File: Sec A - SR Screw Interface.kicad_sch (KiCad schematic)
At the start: 1 part, among them U1 B-B Interface

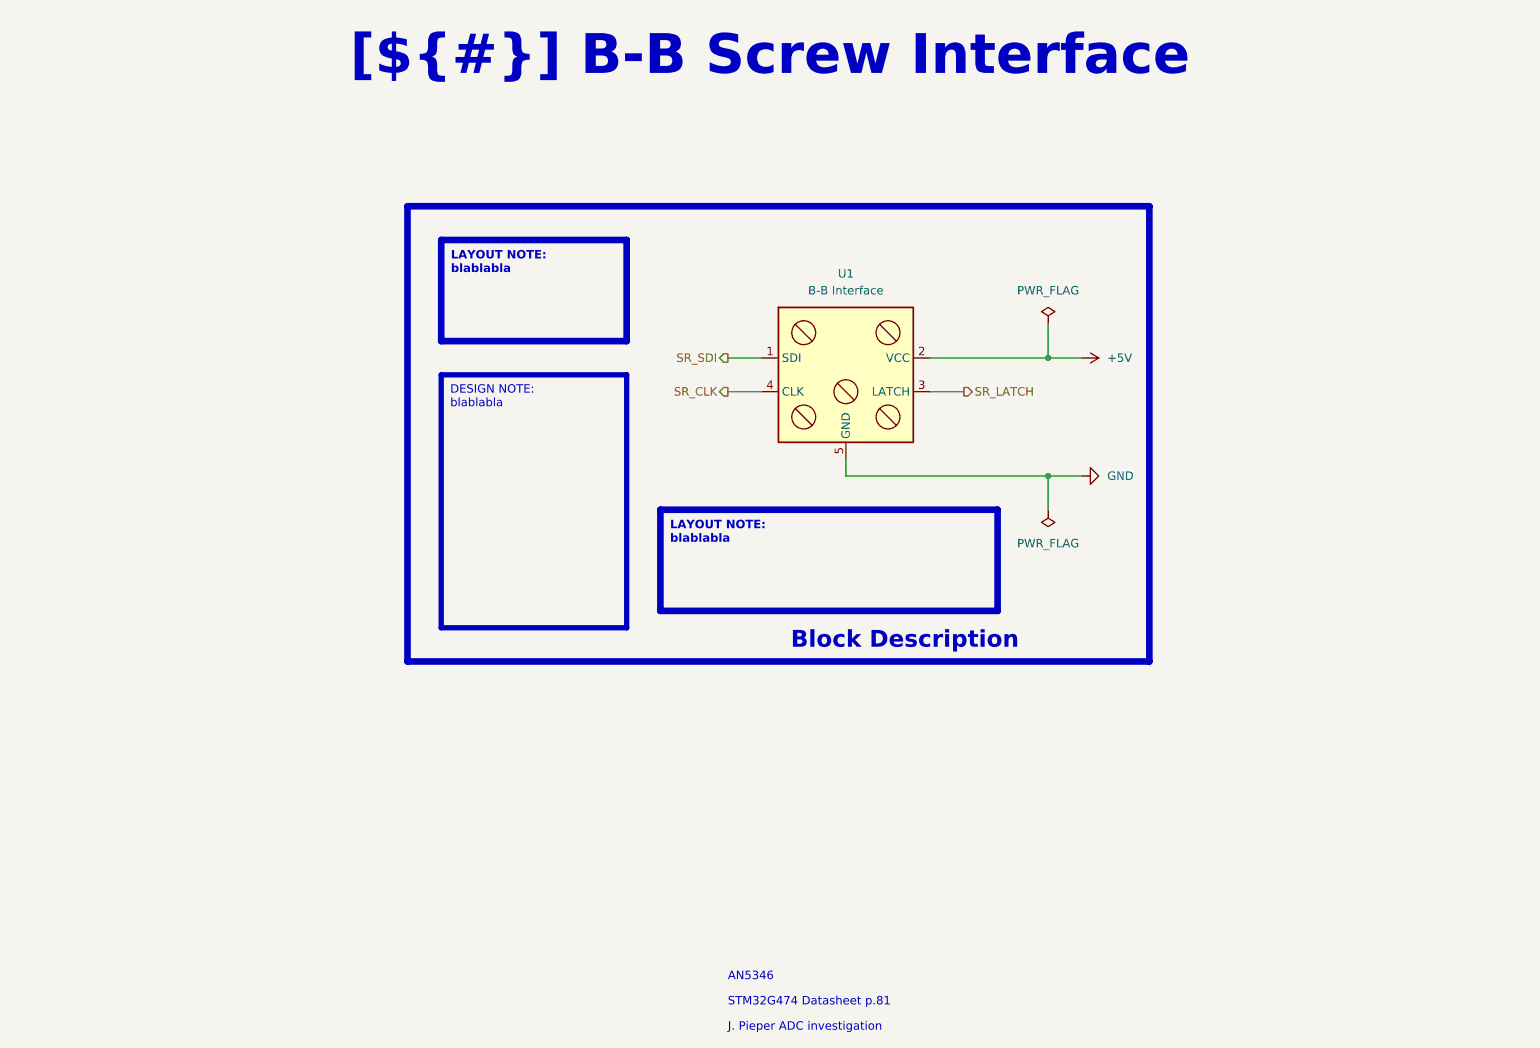
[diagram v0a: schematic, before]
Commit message: documentation update / release 2.1.1 prep
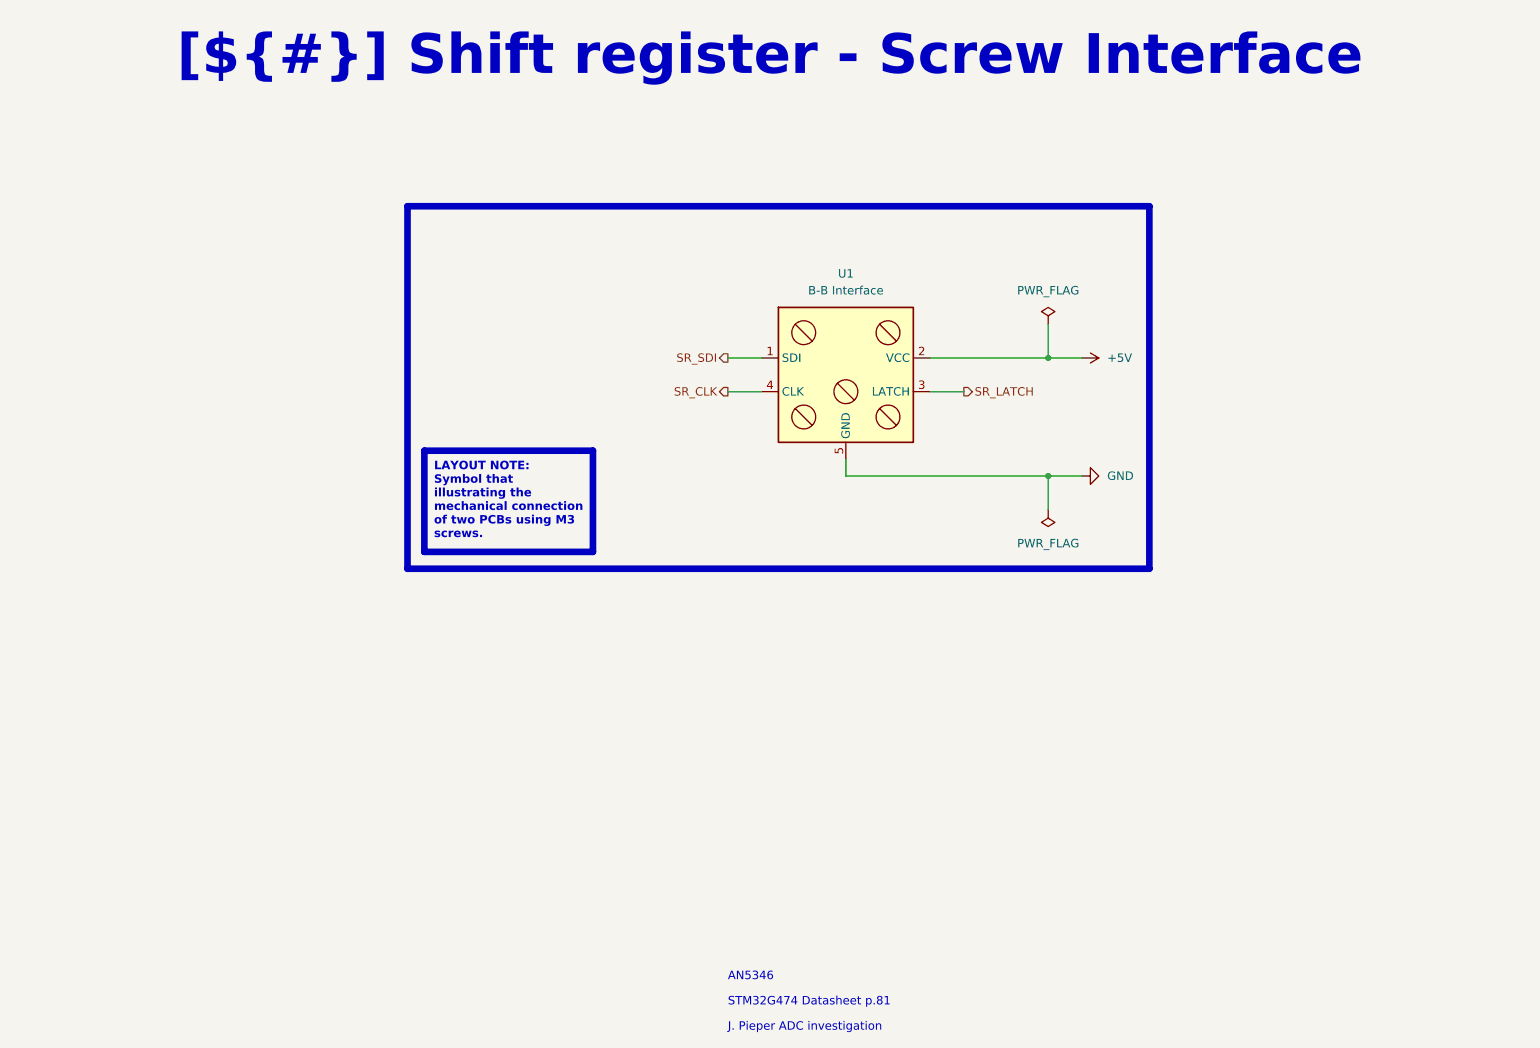
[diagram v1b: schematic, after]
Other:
- title: B-B Screw Interface -> Shift register - Screw Interface
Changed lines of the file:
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@@
 	(paper "A4")
 	(title_block
-		(title "B-B Screw Interface")
+		(title "Shift register - Screw Interface")
 		(date "2025-01-12")
 		(rev "${REVISION}")
@@
 	(rectangle
 		(start 93.98 45.72)
-		(end 205.74 114.3)
+		(end 205.74 100.33)
 		(stroke
 			(width 1)
@@
 		)
 	)
-	(text_box "Block Description"
+	(text_box "LAYOUT NOTE:\nSymbol that illustrating the mechanical connection of two PCBs using M3 screws."
 		(exclude_from_sim no)
-		(at 132.08 106.68 0)
-		(size 73.66 7.62)
-		(margins 1.9049 1.9049 1.9049 1.9049)
-		(stroke
-			(width -0.0001)
-			(type default)
-		)
-		(fill
-			(type none)
-		)
-		(effects
-			(font
-				(face "Times New Roman")
-				(size 2.54 2.54)
-				(thickness 0.508)
-				(bold yes)
-				(color 162 22 34 1)
-			)
-			(justify bottom)
-		)
-	)
-	(text_box "LAYOUT NOTE:\nblablabla"
-		(exclude_from_sim no)
-		(at 132.08 91.44 0)
-		(size 50.8 15.24)
-		(margins 1.4525 1.4525 1.4525 1.4525)
-		(stroke
-			(width 1)
-			(type solid)
-			(color 0 0 255 1)
-		)
-		(fill
-			(type none)
-		)
-		(effects
-			(font
-				(face "Arial")
-				(size 1.27 1.27)
-				(thickness 0.4)
-				(bold yes)
-				(color 0 0 255 1)
-			)
-			(justify left top)
-		)
-	)
-	(text_box "LAYOUT NOTE:\nblablabla"
-		(exclude_from_sim no)
-		(at 99.06 50.8 0)
-		(size 27.94 15.24)
+		(at 96.52 82.55 0)
+		(size 25.4 15.24)
 		(margins 1.4525 1.4525 1.4525 1.4525)
 		(stroke
@@
 		)
 	)
-	(text_box "DESIGN NOTE:\nblablabla"
-		(exclude_from_sim no)
-		(at 99.06 71.12 0)
-		(size 27.94 38.1)
-		(margins 1.3525 1.3525 1.3525 1.3525)
-		(stroke
-			(width 0.8)
-			(type solid)
-			(color 250 236 0 1)
-		)
-		(fill
-			(type none)
-		)
-		(effects
-			(font
-				(face "Arial")
-				(size 1.27 1.27)
-				(color 0 0 0 1)
-			)
-			(justify left top)
-		)
-	)

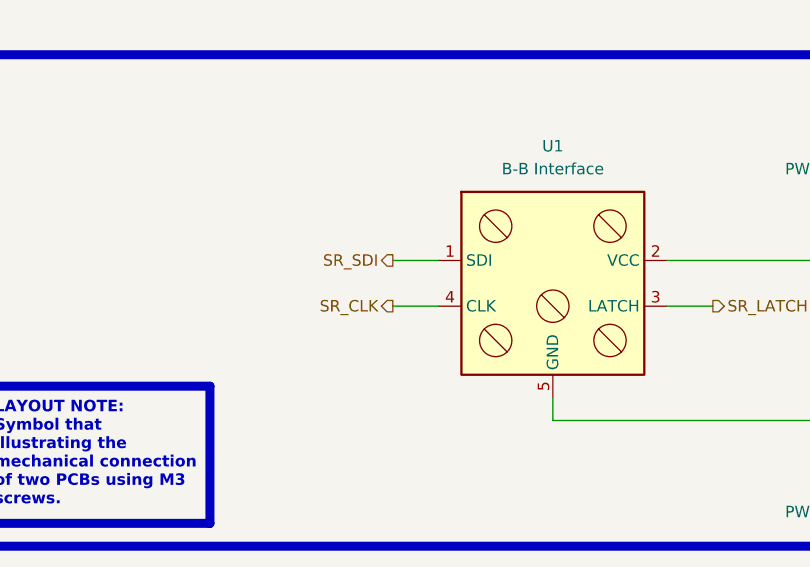
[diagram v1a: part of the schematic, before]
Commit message: fix naming CLK, SDI
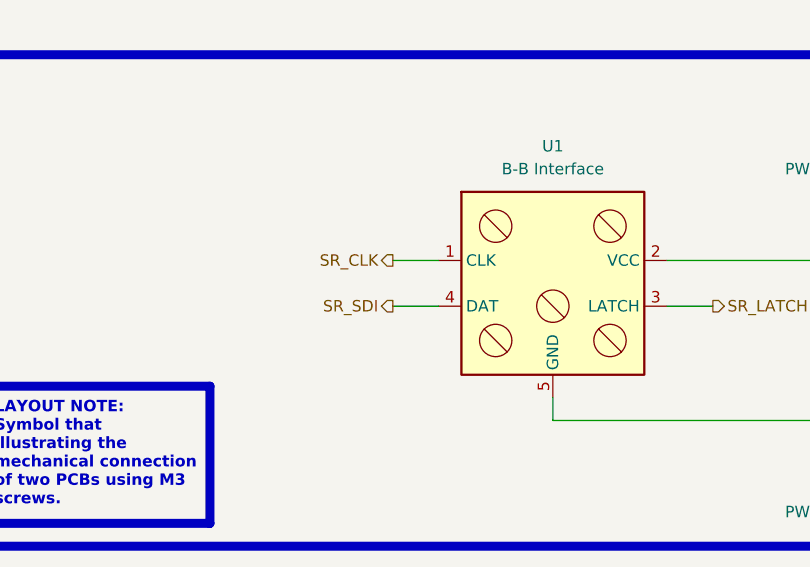
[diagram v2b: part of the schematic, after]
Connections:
- net SR_CLK: now also U1.1 (CLK); no longer U1.4 (CLK)
- net SR_SDI: now also U1.4 (DAT); no longer U1.1 (SDI)
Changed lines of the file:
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@@
 	(wire
 		(pts
-			(xy 142.24 73.66) (xy 147.32 73.66)
+			(xy 142.24 68.58) (xy 147.32 68.58)
 		)
 		(stroke
@@
 	(wire
 		(pts
-			(xy 142.24 68.58) (xy 147.32 68.58)
+			(xy 142.24 73.66) (xy 147.32 73.66)
 		)
 		(stroke
@@
 	(hierarchical_label "SR_CLK"
 		(shape output)
-		(at 142.24 73.66 180)
+		(at 142.24 68.58 180)
 		(effects
 			(font
@@
 	(hierarchical_label "SR_SDI"
 		(shape output)
-		(at 142.24 68.58 180)
+		(at 142.24 73.66 180)
 		(effects
 			(font
